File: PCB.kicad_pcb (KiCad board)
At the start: 4 copper layers, 200 x 150 mm, 518 parts, among them J1 PASSIVE_CHANNELS, J10 USB_RASPBERRY, J11 USB_ARDUINO, J12 100W_ch+, J13 100W_ch-, J14 100W_sense, J15 PowerMosGate, J16 PowerMosDrain, J17 PowerMosSource, J2 PASSIVE_CHANNELS, J3 PASSIVE_CHANNELS, J4 12V+, J5 12V-, J6 5V_PI, J7 5V_PI, J8 ACTIVE_5W_CHANNELS, J9 5V_PI, Q1 BT137-600, Q10 IRLB3813PBF, Q11 IRLB3813PBF, Q12 IRLB3813PbF, Q13 IRLB3813PbF, Q14 IRLB3813PbF, Q15 IRLB3813PbF, Q16 IRLB3813PbF, Q17 IRLB3813PbF, Q2 IRLB3813PbF, Q3 IRLB3813PbF, Q4 IRLB3813PBF, Q5 IRLB3813PBF, Q6 IRLB3813PBF, Q7 IRLB3813PBF, Q8 IRLB3813PBF, Q9 IRLB3813PBF, SW1 RESET_SW, T1+1 TestPoint, T1+2 TestPoint, T1+3 TestPoint, T1+4 TestPoint, T1+5 TestPoint, T1+6 TestPoint, T1+7 TestPoint, T1+8 TestPoint, T1-1 TestPoint, T1-2 TestPoint, T1-3 TestPoint, T1-4 TestPoint, T1-5 TestPoint, T1-6 TestPoint, T1-7 TestPoint, T1-8 TestPoint, T2+1 TestPoint, T2+2 TestPoint, T2+3 TestPoint, T2+4 TestPoint, T2+5 TestPoint, T2+6 TestPoint, T2+7 TestPoint, T2+8 TestPoint, T2-1 TestPoint, T2-2 TestPoint, T2-3 TestPoint, T2-4 TestPoint, T2-5 TestPoint, T2-6 TestPoint, T2-7 TestPoint, T2-8 TestPoint, U1 LM431ACM3_NOPB, U10 INA250A4PW, U11 INA250A4PW, U12 INA250A4PW, U13 ADC124S021CIMM_NOPB, U14 INA250A4PW, U15 INA250A4PW, U16 INA250A4PW, U17 INA250A4PW, U18 ADC124S021CIMM_NOPB, U19 INA250A4PW, U2 LM1117-ADJ, U20 INA250A4PW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

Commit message: Placement canal passif
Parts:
- moved R43 319.5 mm to (164.5, 109.5), turned to 270 degrees
- moved R88 317.2 mm to (162.4, 112.5), turned to 180 degrees
- moved R42 313.6 mm to (164.5, 105.4), turned to 270 degrees
- moved C52 311.1 mm to (152.3, 119.3), turned to 270 degrees
- moved U23 304.0 mm to (157.4, 119.5)
- moved Q6 298.1 mm to (159.2, 114.5)
- moved R51 284.9 mm to (208.5, 109.5), turned to 270 degrees
- moved R50 283.9 mm to (208.5, 105.4), turned to 270 degrees
- moved D8 283.5 mm to (206.5, 91.4)
- moved R92 277.3 mm to (206.4, 112.5), turned to 180 degrees
- moved L8 264.3 mm to (207.2, 72.2)
- moved Q10 258.3 mm to (203.2, 114.5)
- moved R87 253.1 mm to (151.4, 112.5), turned to 180 degrees
- moved U12 246.7 mm to (215.4, 107.6), turned to 90 degrees
- moved C41 245.4 mm to (217.7, 102.5), turned to 180 degrees
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
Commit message: Placement canal actif sauf charge active
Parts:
- moved C1 273.3 mm to (37.1, 175.7)
- moved R2 272.8 mm to (35.2, 168.7)
- moved R1 270.9 mm to (32.4, 168.7)
- moved U1 268.7 mm to (33.8, 163.4), turned to 180 degrees
- moved Q17 264.7 mm to (307.0, 114.5)
- moved Q14 254.4 mm to (274.0, 114.5)
- moved Q15 254.3 mm to (285.0, 114.5)
- moved Q16 253.7 mm to (296.0, 114.5)
- moved Q12 249.7 mm to (252.0, 114.5)
- moved Q13 249.2 mm to (263.0, 114.5)
- moved U3 242.0 mm to (87.2, 140.5)
- moved J5 91.8 mm to (18.9, 157.1)
- moved J4 89.5 mm to (18.9, 170.6)
- moved D1 81.3 mm to (33.5, 178.4)
- moved J10 76.5 mm to (129.3, 207.1), turned to 90 degrees
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
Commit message: Placement première charge active
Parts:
- moved VGS1 12.2 mm to (228.2, 129.9)
- moved VAD2 10.1 mm to (237.2, 118.0)
- moved VGS2 9.55 mm to (244.4, 129.9)
- moved VAD1 6.74 mm to (233.5, 118.1)
- moved V-1 6.26 mm to (227.2, 125.5)
- moved C66 5.78 mm to (244.2, 112.5), turned to 0 degrees
- moved C65 5.32 mm to (233.2, 112.5), turned to 0 degrees
- moved V-2 4.10 mm to (246.5, 126.8)
- moved V+2 3.00 mm to (246.4, 122.9)
- moved V+1 2.20 mm to (227.2, 122.4)
- moved R62 2.06 mm to (228.0, 118.4)
- moved R64 1.69 mm to (231.1, 118.5)
- moved C67 1.19 mm to (237.3, 120.7)
- moved R61 1.14 mm to (241.9, 125.6)
- moved C64 1.02 mm to (240.5, 125.5)
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- renumbered C39 to C38, C40 to C39, C41 to C40, C38 to C41, C44 to C43, C45 to C44, C46 to C45, C43 to C46, C49 to C48, C50 to C49, C51 to C50, C48 to C51, C54 to C53, C55 to C54, C56 to C55, C53 to C56, TPV+3 to TPV+1, TPV-3 to TPV-1, TPVAD3 to TPVAD1, TPVGS3 to TPVGS1, U11 to U10, U12 to U11, U9 to U12, U15 to U14, U16 to U15, U17 to U16, U14 to U17, U20 to U19, U21 to U20, U22 to U21, U19 to U22, U25 to U24, U26 to U25, U27 to U26, U24 to U27, U10 to U9, TPV+1 to V+1, TPV+2 to V+2, TPV+4 to V+3, TPV+5 to V+4, TPV+6 to V+5, TPV+7 to V+6, TPV+8 to V+7, TPV+9 to V+8, TPV-1 to V-1, TPV-2 to V-2, TPV-4 to V-3, TPV-5 to V-4, TPV-6 to V-5, TPV-7 to V-6, TPV-8 to V-7, TPV-9 to V-8, TPVAD1 to VAD1, TPVAD2 to VAD2, TPVAD4 to VAD3, TPVAD5 to VAD4, TPVAD6 to VAD5, TPVAD7 to VAD6, TPVAD8 to VAD7, TPVAD9 to VAD8, TPVGS1 to VGS1, TPVGS2 to VGS2, TPVGS4 to VGS3, TPVGS5 to VGS4, TPVGS6 to VGS5, TPVGS7 to VGS6, TPVGS8 to VGS7, TPVGS9 to VGS8

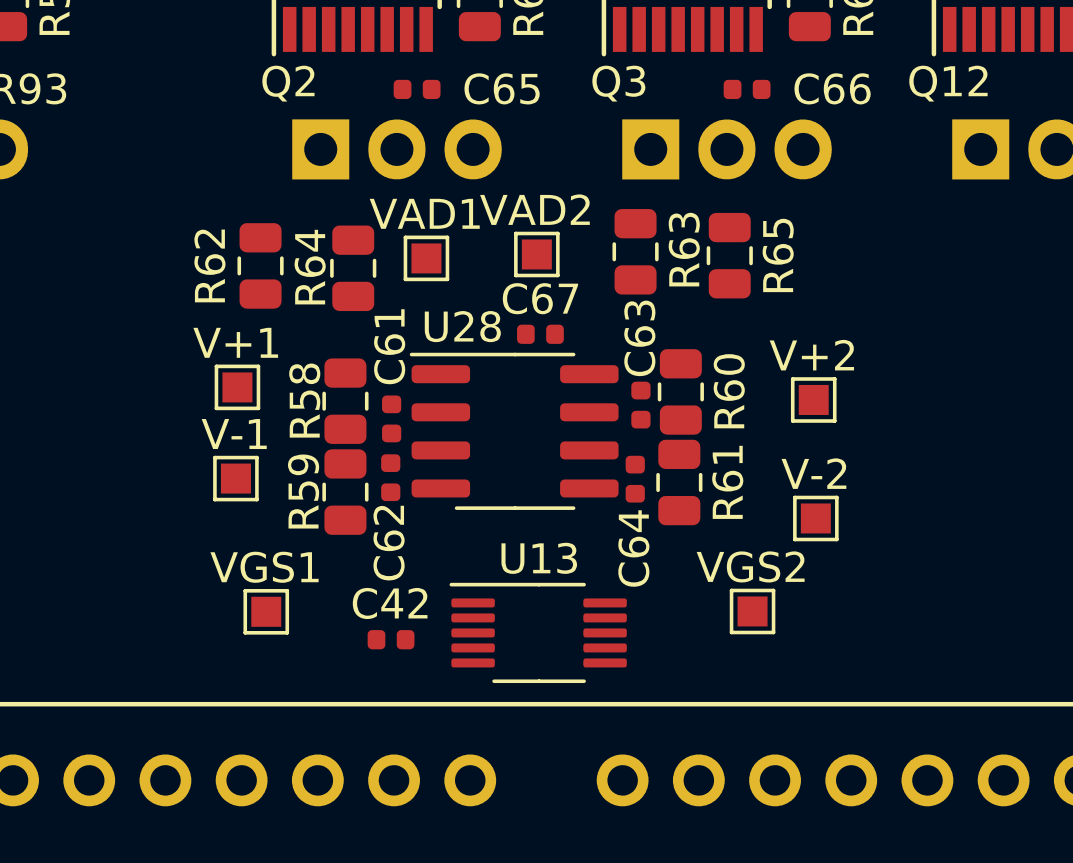
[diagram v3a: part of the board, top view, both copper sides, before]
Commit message: Placement première charge active 2nd try
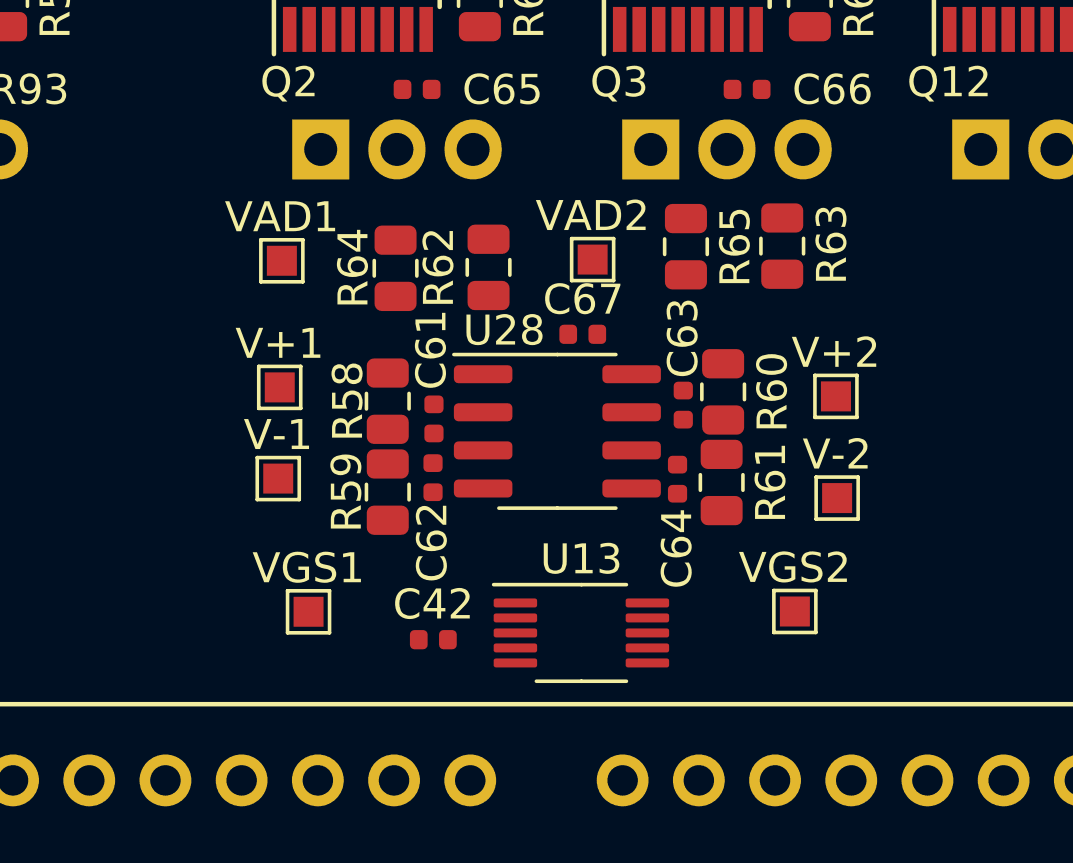
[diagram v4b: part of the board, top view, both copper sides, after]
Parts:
- moved R62 7.60 mm to (235.6, 118.4)
- moved R63 4.89 mm to (245.4, 117.7)
- moved VAD1 4.82 mm to (228.7, 118.2)
- moved VAD2 1.87 mm to (239.1, 118.2)
- moved R65 1.49 mm to (242.2, 117.8)
- moved C63 1.41 mm to (242.1, 123.0)
- moved R61 1.41 mm to (243.4, 125.6)
- moved V-1 1.41 mm to (228.6, 125.5)
- moved VGS2 1.41 mm to (245.8, 129.9)
- moved C42 1.41 mm to (233.8, 130.8)
- moved C61 1.41 mm to (233.8, 123.5)
- moved C62 1.41 mm to (233.7, 125.5)
- moved C64 1.41 mm to (241.9, 125.5)
- moved C67 1.41 mm to (238.7, 120.7)
- moved R58 1.41 mm to (232.2, 122.9)
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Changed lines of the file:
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@@
   )
   (module Capacitor_SMD:C_0402_1005Metric (layer F.Cu)
-    (at 240.48 125.5 90)
+    (at 241.89 125.5 90)
     (descr "Capacitor SMD 0402 (1005 Metric), square (rectangular) end terminal, IPC_7351 nominal, (Body size source: http://www.tortai-tech.com/upload/download/2011102023233369053.pdf), generated with kicad-footprint-generator")
     (tags capacitor)
@@
   )
   (module Capacitor_SMD:C_0402_1005Metric (layer F.Cu)
-    (at 232.34 130.85)
+    (at 233.75 130.85)
     (descr "Capacitor SMD 0402 (1005 Metric), square (rectangular) end terminal, IPC_7351 nominal, (Body size source: http://www.tortai-tech.com/upload/download/2011102023233369053.pdf), generated with kicad-footprint-generator")
     (tags capacitor)
@@
   )
   (module Capacitor_SMD:C_0402_1005Metric (layer F.Cu)
-    (at 232.36 123.49 90)
+    (at 233.77 123.49 90)
     (descr "Capacitor SMD 0402 (1005 Metric), square (rectangular) end terminal, IPC_7351 nominal, (Body size source: http://www.tortai-tech.com/upload/download/2011102023233369053.pdf), generated with kicad-footprint-generator")
     (tags capacitor)
     (attr smd)
-    (fp_text reference C61 (at 2.43 -0.03 90) (layer F.SilkS)
+    (fp_text reference C61 (at 2.31 -0.08 90) (layer F.SilkS)
       (effects (font (size 1 1) (thickness 0.15)))
     )
@@
   )
   (module Capacitor_SMD:C_0402_1005Metric (layer F.Cu)
-    (at 232.33 125.45 90)
+    (at 233.74 125.45 90)
     (descr "Capacitor SMD 0402 (1005 Metric), square (rectangular) end terminal, IPC_7351 nominal, (Body size source: http://www.tortai-tech.com/upload/download/2011102023233369053.pdf), generated with kicad-footprint-generator")
     (tags capacitor)
@@
   )
   (module Capacitor_SMD:C_0402_1005Metric (layer F.Cu)
-    (at 240.67 123.03 90)
+    (at 242.08 123.03 90)
     (descr "Capacitor SMD 0402 (1005 Metric), square (rectangular) end terminal, IPC_7351 nominal, (Body size source: http://www.tortai-tech.com/upload/download/2011102023233369053.pdf), generated with kicad-footprint-generator")
     (tags capacitor)
@@
   )
   (module Capacitor_SMD:C_0402_1005Metric (layer F.Cu)
-    (at 237.32 120.67)
+    (at 238.73 120.67)
     (descr "Capacitor SMD 0402 (1005 Metric), square (rectangular) end terminal, IPC_7351 nominal, (Body size source: http://www.tortai-tech.com/upload/download/2011102023233369053.pdf), generated with kicad-footprint-generator")
     (tags capacitor)
@@
   )
   (module Resistor_SMD:R_0805_2012Metric (layer F.Cu)
-    (at 230.82 122.9 270)
+    (at 232.23 122.9 270)
     (descr "Resistor SMD 0805 (2012 Metric), square (rectangular) end terminal, IPC_7351 nominal, (Body size source: https://docs.google.com/spreadsheets/d/1BsfQQcO9C6DZCsRaXUlFlo91Tg2WpOkGARC1WS5S8t0/edit?usp=sharing), generated with kicad-footprint-generator")
     (tags resistor)
@@
   )
   (module Resistor_SMD:R_0805_2012Metric (layer F.Cu)
-    (at 230.82 125.93 270)
+    (at 232.23 125.93 270)
     (descr "Resistor SMD 0805 (2012 Metric), square (rectangular) end terminal, IPC_7351 nominal, (Body size source: https://docs.google.com/spreadsheets/d/1BsfQQcO9C6DZCsRaXUlFlo91Tg2WpOkGARC1WS5S8t0/edit?usp=sharing), generated with kicad-footprint-generator")
     (tags resistor)
@@
   )
   (module Resistor_SMD:R_0805_2012Metric (layer F.Cu)
-    (at 242 122.59 270)
+    (at 243.41 122.59 270)
     (descr "Resistor SMD 0805 (2012 Metric), square (rectangular) end terminal, IPC_7351 nominal, (Body size source: https://docs.google.com/spreadsheets/d/1BsfQQcO9C6DZCsRaXUlFlo91Tg2WpOkGARC1WS5S8t0/edit?usp=sharing), generated with kicad-footprint-generator")
     (tags resistor)
@@
   )
   (module Resistor_SMD:R_0805_2012Metric (layer F.Cu)
-    (at 241.95 125.61 270)
+    (at 243.36 125.61 270)
     (descr "Resistor SMD 0805 (2012 Metric), square (rectangular) end terminal, IPC_7351 nominal, (Body size source: https://docs.google.com/spreadsheets/d/1BsfQQcO9C6DZCsRaXUlFlo91Tg2WpOkGARC1WS5S8t0/edit?usp=sharing), generated with kicad-footprint-generator")
     (tags resistor)
@@
   )
   (module Resistor_SMD:R_0805_2012Metric (layer F.Cu)
-    (at 227.99 118.39 90)
+    (at 235.59 118.44 90)
     (descr "Resistor SMD 0805 (2012 Metric), square (rectangular) end terminal, IPC_7351 nominal, (Body size source: https://docs.google.com/spreadsheets/d/1BsfQQcO9C6DZCsRaXUlFlo91Tg2WpOkGARC1WS5S8t0/edit?usp=sharing), generated with kicad-footprint-generator")
     (tags resistor)
@@
   )
   (module Resistor_SMD:R_0805_2012Metric (layer F.Cu)
-    (at 240.49 117.92 90)
+    (at 245.38 117.73 90)
     (descr "Resistor SMD 0805 (2012 Metric), square (rectangular) end terminal, IPC_7351 nominal, (Body size source: https://docs.google.com/spreadsheets/d/1BsfQQcO9C6DZCsRaXUlFlo91Tg2WpOkGARC1WS5S8t0/edit?usp=sharing), generated with kicad-footprint-generator")
     (tags resistor)
@@
   )
   (module Resistor_SMD:R_0805_2012Metric (layer F.Cu)
-    (at 231.08 118.47 270)
+    (at 232.49 118.47 270)
     (descr "Resistor SMD 0805 (2012 Metric), square (rectangular) end terminal, IPC_7351 nominal, (Body size source: https://docs.google.com/spreadsheets/d/1BsfQQcO9C6DZCsRaXUlFlo91Tg2WpOkGARC1WS5S8t0/edit?usp=sharing), generated with kicad-footprint-generator")
     (tags resistor)
@@
   )
   (module Resistor_SMD:R_0805_2012Metric (layer F.Cu)
-    (at 243.63 118.05 270)
+    (at 242.17 117.75 270)
     (descr "Resistor SMD 0805 (2012 Metric), square (rectangular) end terminal, IPC_7351 nominal, (Body size source: https://docs.google.com/spreadsheets/d/1BsfQQcO9C6DZCsRaXUlFlo91Tg2WpOkGARC1WS5S8t0/edit?usp=sharing), generated with kicad-footprint-generator")
     (tags resistor)
@@
   )
   (module TestPoint:TestPoint_Pad_1.0x1.0mm (layer F.Cu)
-    (at 227.22 122.44)
+    (at 228.63 122.44)
     (descr "SMD rectangular pad as test Point, square 1.0mm side length")
     (tags "test point SMD pad rectangle square")
@@
   )
   (module TestPoint:TestPoint_Pad_1.0x1.0mm (layer F.Cu)
-    (at 246.43 122.86)
+    (at 247.17 122.74)
     (descr "SMD rectangular pad as test Point, square 1.0mm side length")
     (tags "test point SMD pad rectangle square")
@@
   )
   (module TestPoint:TestPoint_Pad_1.0x1.0mm (layer F.Cu)
-    (at 227.17 125.48)
+    (at 228.58 125.48)
     (descr "SMD rectangular pad as test Point, square 1.0mm side length")
     (tags "test point SMD pad rectangle square")
@@
   )
   (module TestPoint:TestPoint_Pad_1.0x1.0mm (layer F.Cu)
-    (at 246.5 126.81)
+    (at 247.21 126.13)
     (descr "SMD rectangular pad as test Point, square 1.0mm side length")
     (tags "test point SMD pad rectangle square")
@@
   )
   (module TestPoint:TestPoint_Pad_1.0x1.0mm (layer F.Cu)
-    (at 233.52 118.14)
+    (at 228.7 118.22)
     (descr "SMD rectangular pad as test Point, square 1.0mm side length")
     (tags "test point SMD pad rectangle square")
@@
   )
   (module TestPoint:TestPoint_Pad_1.0x1.0mm (layer F.Cu)
-    (at 237.2 118.01)
+    (at 239.06 118.18)
     (descr "SMD rectangular pad as test Point, square 1.0mm side length")
     (tags "test point SMD pad rectangle square")
@@
   )
   (module TestPoint:TestPoint_Pad_1.0x1.0mm (layer F.Cu)
-    (at 228.18 129.92)
+    (at 229.59 129.92)
     (descr "SMD rectangular pad as test Point, square 1.0mm side length")
     (tags "test point SMD pad rectangle square")
@@
   )
   (module TestPoint:TestPoint_Pad_1.0x1.0mm (layer F.Cu)
-    (at 244.39 129.91)
+    (at 245.8 129.91)
     (descr "SMD rectangular pad as test Point, square 1.0mm side length")
     (tags "test point SMD pad rectangle square")
@@
   )
   (module Package_SO:VSSOP-10_3x3mm_P0.5mm (layer F.Cu)
-    (at 237.275 130.625)
+    (at 238.685 130.625)
     (descr "VSSOP, 10 Pin (http://www.ti.com/lit/ds/symlink/ads1115.pdf), generated with kicad-footprint-generator ipc_gullwing_generator.py")
     (tags "VSSOP SO")
@@
   )
   (module Package_SO:SOIC-8_3.9x4.9mm_P1.27mm (layer F.Cu)
-    (at 236.475 123.905)
+    (at 237.885 123.905)
     (descr "SOIC, 8 Pin (JEDEC MS-012AA, https://www.analog.com/media/en/package-pcb-resources/package/pkg_pdf/soic_narrow-r/r_8.pdf), generated with kicad-footprint-generator ipc_gullwing_generator.py")
     (tags "SOIC SO")
     (attr smd)
-    (fp_text reference U28 (at -1.755 -3.455) (layer F.SilkS)
+    (fp_text reference U28 (at -1.775 -3.355) (layer F.SilkS)
       (effects (font (size 1 1) (thickness 0.15)))
     )

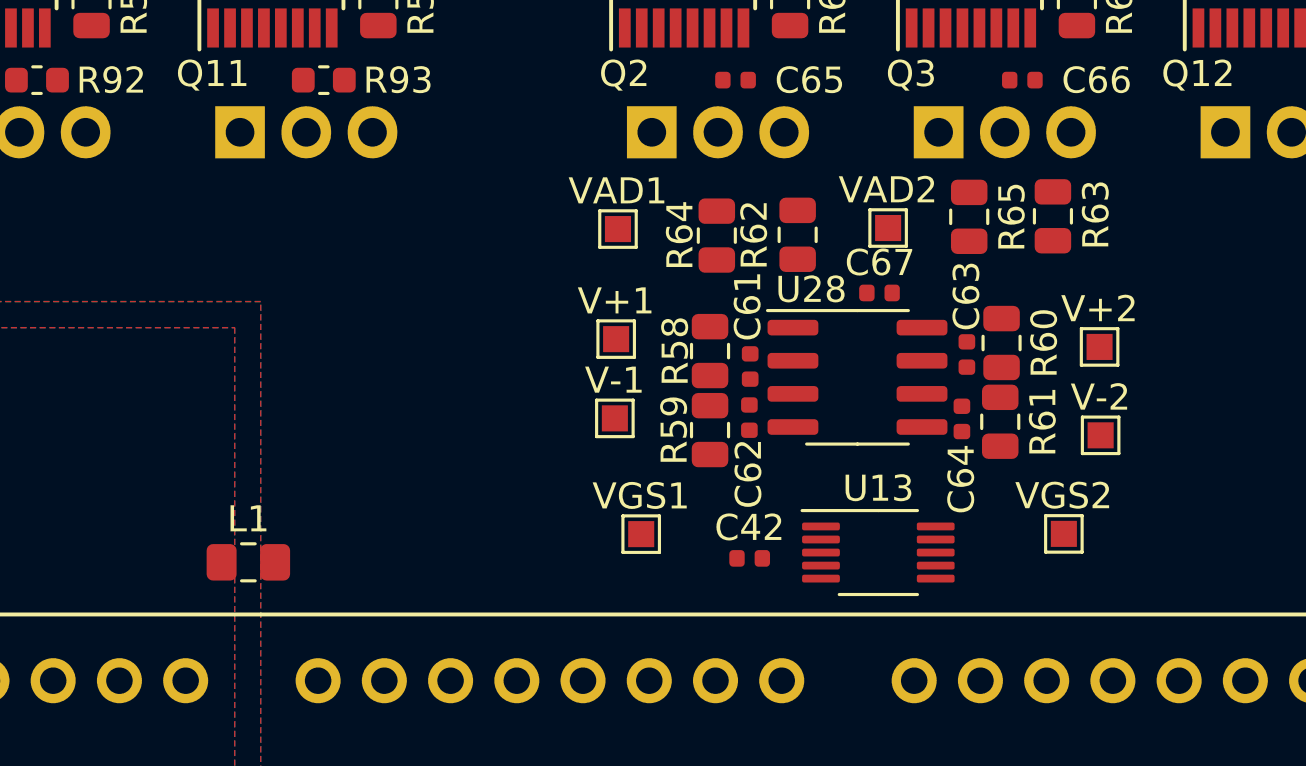
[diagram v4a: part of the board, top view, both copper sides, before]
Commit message: Placement première charge active, pret a dupliquer
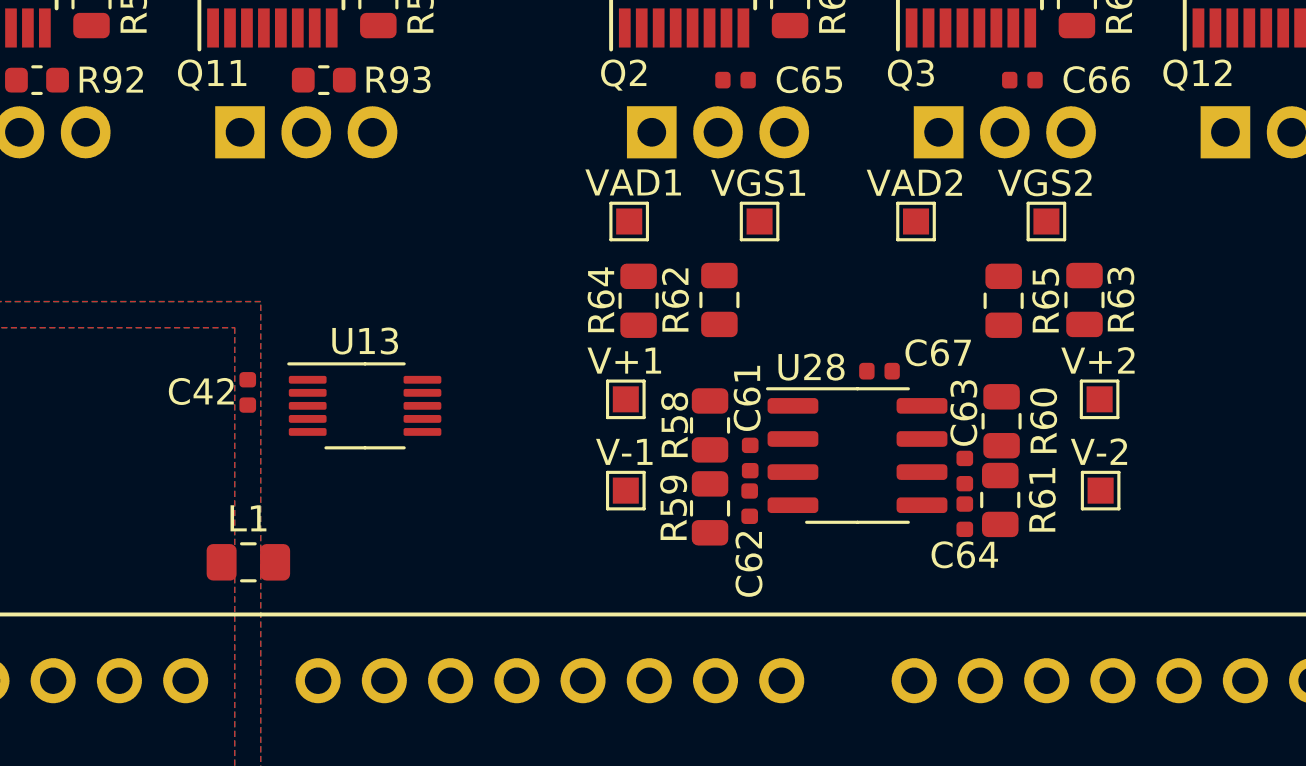
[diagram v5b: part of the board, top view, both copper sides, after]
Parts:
- moved U13 20.5 mm to (219.0, 125.0)
- moved C42 20.3 mm to (214.5, 124.5), turned to 270 degrees
- moved VGS1 12.8 mm to (234.1, 117.9)
- moved VGS2 12.0 mm to (245.1, 117.9)
- moved C63 4.47 mm to (242.0, 127.5)
- moved R62 3.91 mm to (232.6, 120.9)
- moved R64 3.91 mm to (229.5, 121.0)
- moved C64 3.75 mm to (242.0, 129.2)
- moved C61 3.51 mm to (233.8, 127.0)
- moved R65 3.48 mm to (243.5, 121.0)
- moved R63 3.43 mm to (246.6, 120.9)
- moved C62 3.30 mm to (233.8, 128.8)
- moved R61 3.00 mm to (243.4, 128.6)
- moved C67 3.00 mm to (238.7, 123.7)
- moved R59 3.00 mm to (232.2, 128.9)
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
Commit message: Charge actives dupliques, placement filtres rc
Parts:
- moved R138 388.1 mm to (366.2, 209.9), turned to 270 degrees
- moved R136 388.0 mm to (366.2, 215.9), turned to 270 degrees
- moved C105 384.3 mm to (366.0, 212.9)
- moved R137 384.1 mm to (362.7, 215.8), turned to 270 degrees
- moved R139 380.7 mm to (363.2, 209.9), turned to 270 degrees
- moved C106 380.0 mm to (362.9, 212.9), turned to 180 degrees
- moved C107 379.9 mm to (366.0, 206.9)
- moved C108 376.4 mm to (363.0, 206.9), turned to 180 degrees
- moved R161 361.3 mm to (354.8, 195.3), turned to 270 degrees
- moved R160 361.0 mm to (358.3, 195.4), turned to 270 degrees
- moved R149 359.7 mm to (341.9, 194.3), turned to 270 degrees
- moved R162 353.6 mm to (358.3, 189.4), turned to 270 degrees
- moved C128 351.7 mm to (355.0, 192.4), turned to 180 degrees
- moved R150 350.9 mm to (345.4, 188.4), turned to 270 degrees
- moved R148 349.8 mm to (345.4, 194.4), turned to 270 degrees
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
